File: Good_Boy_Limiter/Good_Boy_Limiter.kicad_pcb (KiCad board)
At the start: 2 copper layers, 7 parts, among them Q2 AO3422, U1 ESP32-S3-WROOM-1, U2 TC4427EOA_C636891, U3 XL7015E1

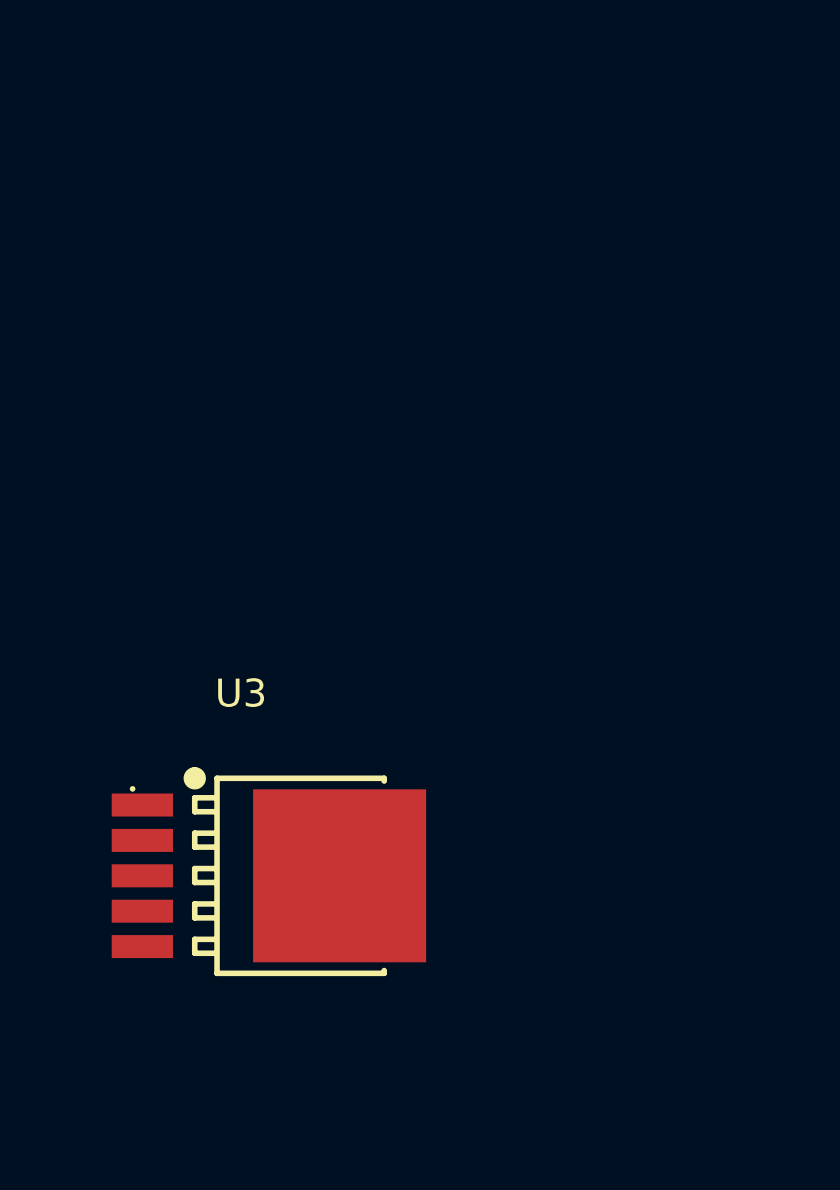
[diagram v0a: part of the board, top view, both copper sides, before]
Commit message: Added schottky and Inductor for DC-DC converter
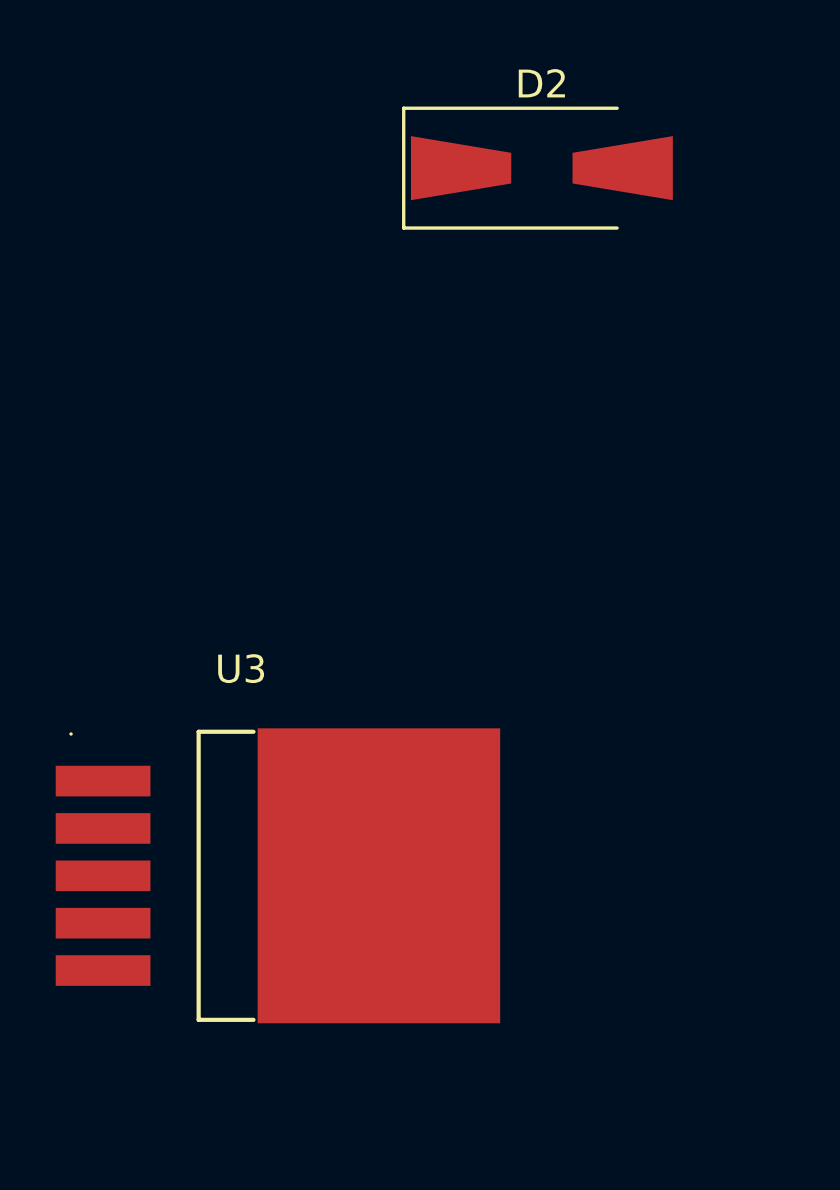
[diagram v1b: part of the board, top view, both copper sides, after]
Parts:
- added D2: SS36, Diode_SMD:D_SMA-SMB_Universal_Handsoldering, F.Cu at (47.9, 30.5)
- U3: value XL7015E1 -> LM2576HVR-12; footprint easyeda2kicad:TO-252-5_L6.6-W5.8-P1.27-TL -> easyeda2kicad:TO-263-5_L10.2-W8.6-P1.70-LS14.4-TL
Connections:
- C1 pad 1: unconnected-(C1-Pad1) -> /GPIO1
- C1 pad 2: unconnected-(C1-Pad2) -> GND
- Q2 pad 1: unconnected-(Q2-G-Pad1) -> Net-(Q2-G)
- Q2 pad 2: unconnected-(Q2-S-Pad2) -> +48VOUT
- Q2 pad 3: unconnected-(Q2-D-Pad3) -> Net-(Q2-D)
- R1 pad 1: unconnected-(R1-Pad1) -> GND
- R1 pad 2: unconnected-(R1-Pad2) -> /GPIO1
- R2 pad 2: unconnected-(R2-Pad2) -> /GPIO1
- U1 pad 1: Net-(U1-GND-Pad1) -> GND
- U1 pad 38: unconnected-(U1-IO2-Pad38) -> /GPIO2
- U1 pad 39: unconnected-(U1-IO1-Pad39) -> /GPIO1
- U1 pad 40: Net-(U1-GND-Pad1) -> GND
- U1 pad 41: Net-(U1-GND-Pad1) -> GND
- U2 pad 2: unconnected-(U2-INA-Pad2) -> /GPIO2
- U2 pad 3: unconnected-(U2-GND-Pad3) -> GND
- U2 pad 6: unconnected-(U2-VDD-Pad6) -> /+12V
- U2 pad 7: unconnected-(U2-OUTA-Pad7) -> Net-(U2-OUTA)
- U3 pad 1: unconnected-(U3-VIN-Pad1) -> +48VIN
- U3 pad 2: unconnected-(U3-SW-Pad2) -> Net-(D2-K)
- U3 pad 3: unconnected-(U3-GND-Pad3) -> GND
- U3 pad 4: unconnected-(U3-FB-Pad4) -> /+12V
- U3 pad 5: unconnected-(U3-EN-Pad5) -> GND
- U3 pad 6: unconnected-(U3-GND-Pad6) -> GND

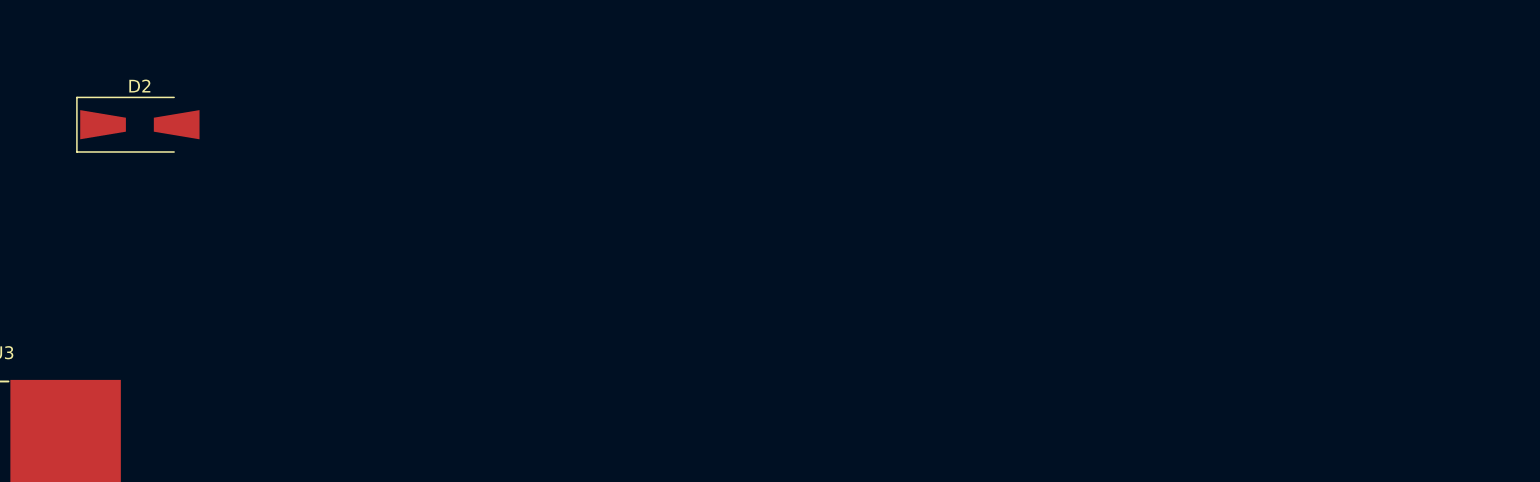
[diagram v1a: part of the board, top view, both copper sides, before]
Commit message: FIX: Added capacitors for Buck
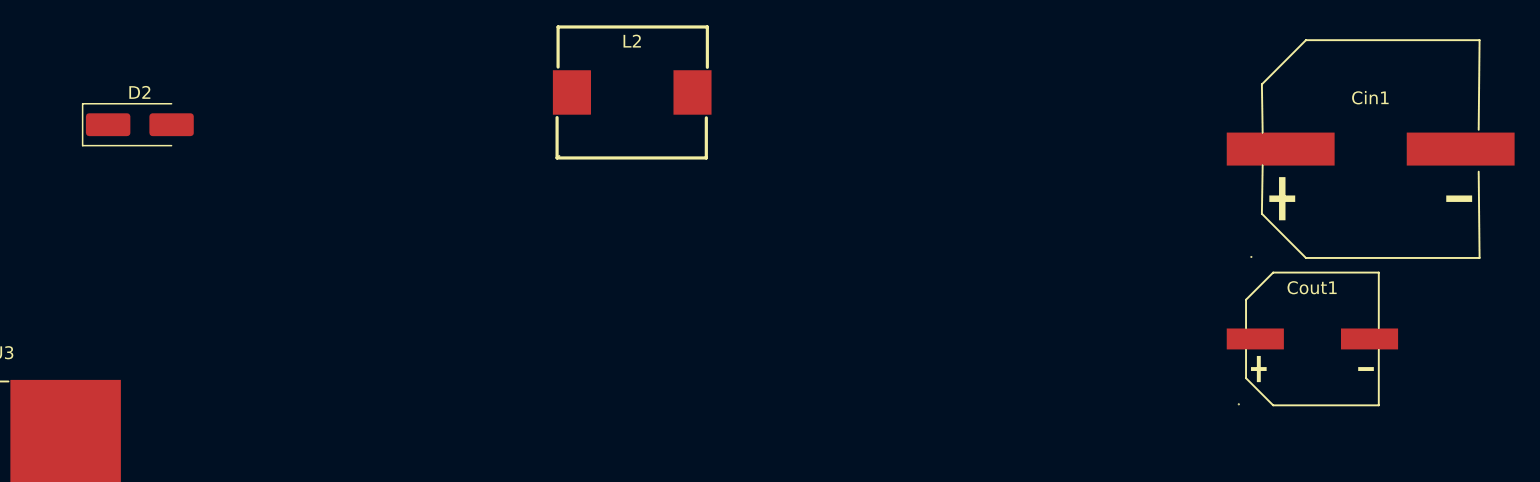
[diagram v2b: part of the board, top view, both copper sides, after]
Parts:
- added Cin1: 100uF, easyeda2kicad:CAP-SMD_BD16.0-L17.0-W17.0-FD, F.Cu at (144.9, 32.4)
- added Cout1: 1000uF, easyeda2kicad:CAP-SMD_BD10.0-L10.3-W10.3-FD, F.Cu at (140.3, 47.4)
- added L2: SL1050-101M, easyeda2kicad:IND-SMD_L11.5-W10.5, F.Cu at (86.7, 27.9)
- D2: footprint Diode_SMD:D_SMA-SMB_Universal_Handsoldering -> Diode_SMD:D_SMA_Handsoldering

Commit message: Added a lot of stuff, sowwy
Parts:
- added Cin2: 100uF, easyeda2kicad:CAP-SMD_BD16.0-L17.0-W17.0-FD, F.Cu at (57.0, 122.2)
- added Cout2: 1000uF, easyeda2kicad:CAP-SMD_BD10.0-L10.3-W10.3-FD, F.Cu at (69.2, 137.2)
- added D3: SS36, Diode_SMD:D_SMA_Handsoldering, F.Cu at (73.9, 126.9)
- added D4: 1N4148W, Diode_SMD:D_SOD-123, F.Cu at (133.5, 87.1)
- added D7: LED, LED_SMD:LED_0805_2012Metric_Pad1.15x1.40mm_HandSolder, F.Cu at (129.4, 97.3)
- added D8: LED, LED_SMD:LED_0805_2012Metric_Pad1.15x1.40mm_HandSolder, F.Cu at (129.4, 100.3)
- added L3: SL1050-101M, easyeda2kicad:IND-SMD_L11.5-W10.5, F.Cu at (75.6, 118.8)
- added U4: LM2576SX-3.3/NOPB, easyeda2kicad:TO-263-5_L10.2-W8.9-P1.70-TL, F.Cu at (52.3, 137.4)
- added U5: MAX40200AUK+T, easyeda2kicad:TSOT-23-5_L2.9-W1.6-P0.95-LS2.8-BL, F.Cu at (133.0, 90.9)
- added U6: AMS1117-3.3, Package_TO_SOT_SMD:SOT-223-3_TabPin2, F.Cu at (125.6, 89.6)
- added U7: MAX40200AUK+T, easyeda2kicad:TSOT-23-5_L2.9-W1.6-P0.95-LS2.8-BL, F.Cu at (136.2, 97.9)
- added U9: LM393DR2G, easyeda2kicad:SOIC-8_L5.0-W4.0-P1.27-LS6.0-BL, F.Cu at (123.8, 99.9)
- added USB1: USB-TYPE-C-018, easyeda2kicad:USB-C_SMD-TYPE-C-31-M-12, F.Cu at (126.1, 79.7)
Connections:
- U1 pad 13: unconnected-(U1-USB_D--Pad13) -> /D-
- U1 pad 14: unconnected-(U1-USB_D+-Pad14) -> /D+
- U1 pad 2: unconnected-(U1-3V3-Pad2) -> /3V3
- U1 pad 27: unconnected-(U1-IO0-Pad27) -> /GPIO0
- U1 pad 3: unconnected-(U1-EN-Pad3) -> Net-(U1-EN)

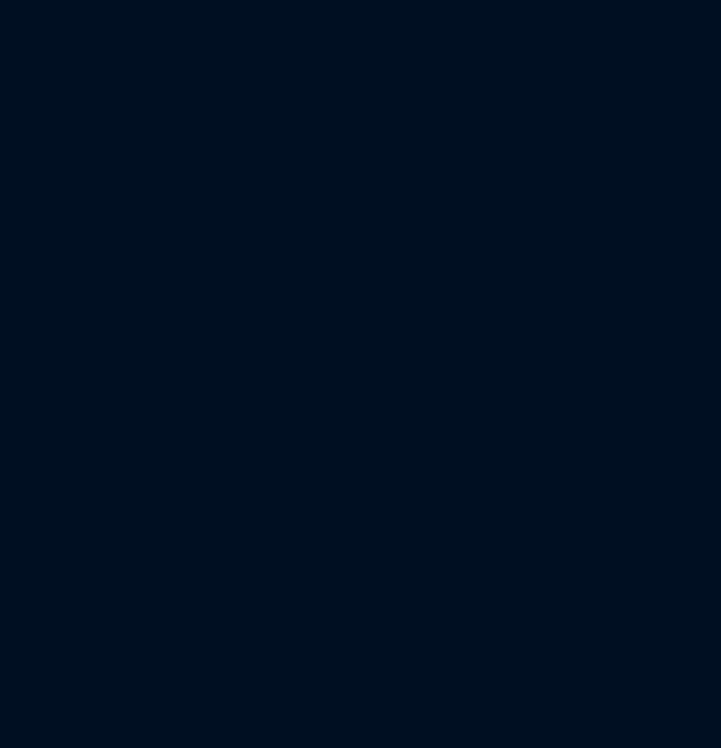
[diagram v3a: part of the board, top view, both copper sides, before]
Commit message: Added some footprints
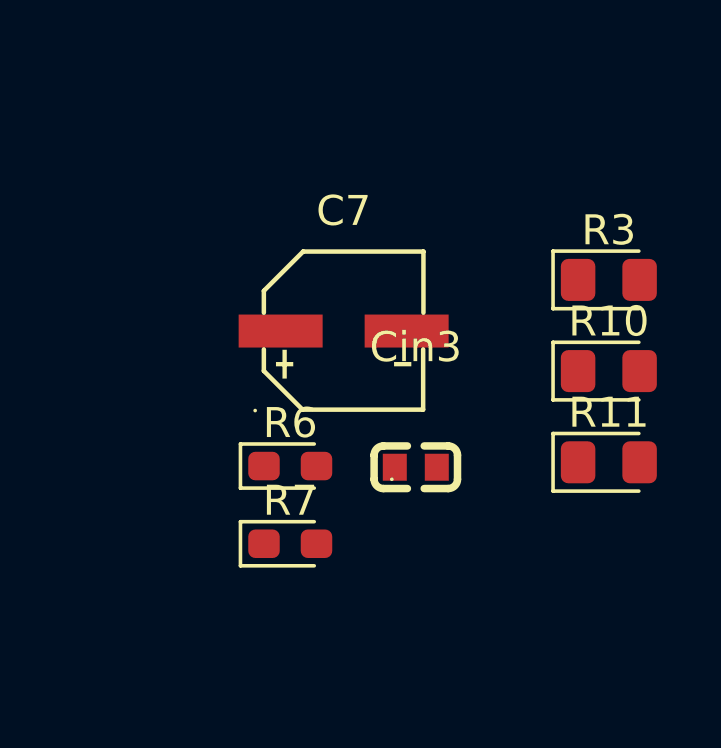
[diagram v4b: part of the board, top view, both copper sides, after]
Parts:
- added C7: 22uF, easyeda2kicad:CAP-SMD_BD5.0-L5.3-W5.3-FD, F.Cu at (165.4, 64.2)
- added Cin3: 10uF, easyeda2kicad:C0603, F.Cu at (167.8, 68.7)
- added R10: 330, LED_SMD:LED_0805_2012Metric_Pad1.15x1.40mm_HandSolder, F.Cu at (174.2, 65.5)
- added R11: 330, LED_SMD:LED_0805_2012Metric_Pad1.15x1.40mm_HandSolder, F.Cu at (174.2, 68.6)
- added R3: 10, LED_SMD:LED_0805_2012Metric_Pad1.15x1.40mm_HandSolder, F.Cu at (174.2, 62.5)
- added R6: 5.1K, LED_SMD:LED_0603_1608Metric_Pad1.05x0.95mm_HandSolder, F.Cu at (163.6, 68.7)
- added R7: 5.1K, LED_SMD:LED_0603_1608Metric_Pad1.05x0.95mm_HandSolder, F.Cu at (163.6, 71.3)

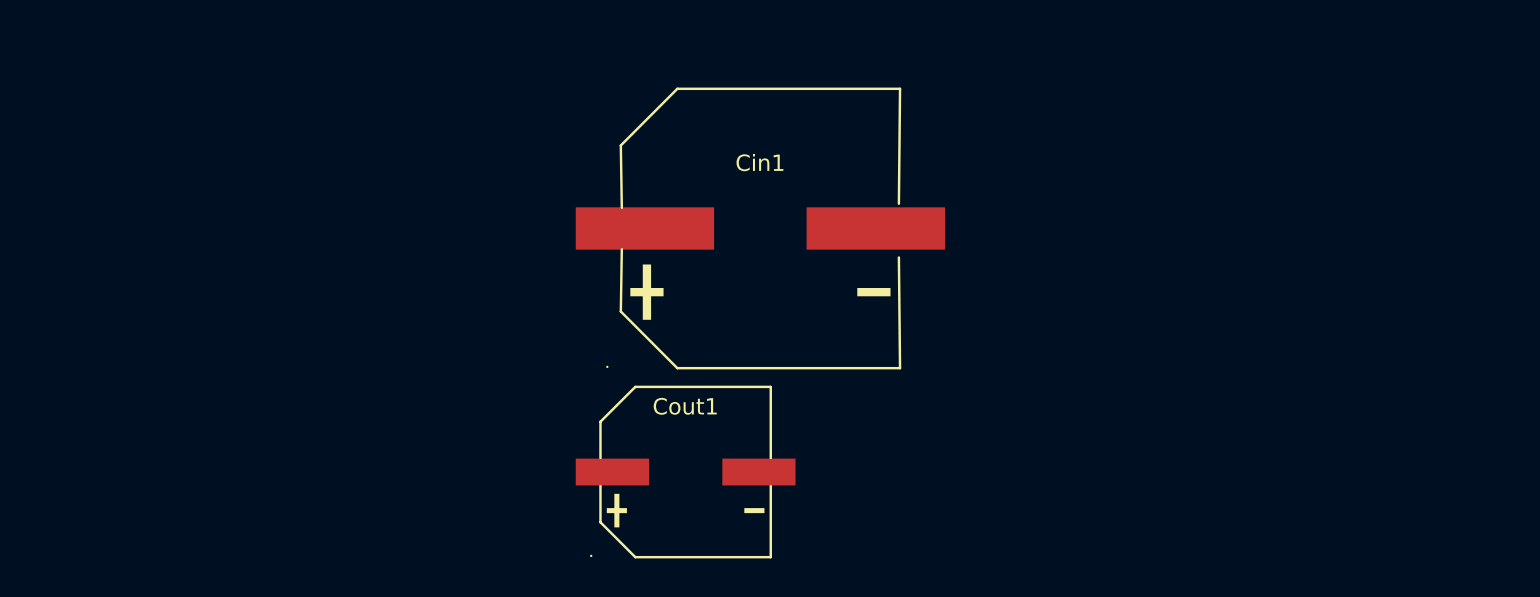
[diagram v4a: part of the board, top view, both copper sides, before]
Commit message: Added more footprints
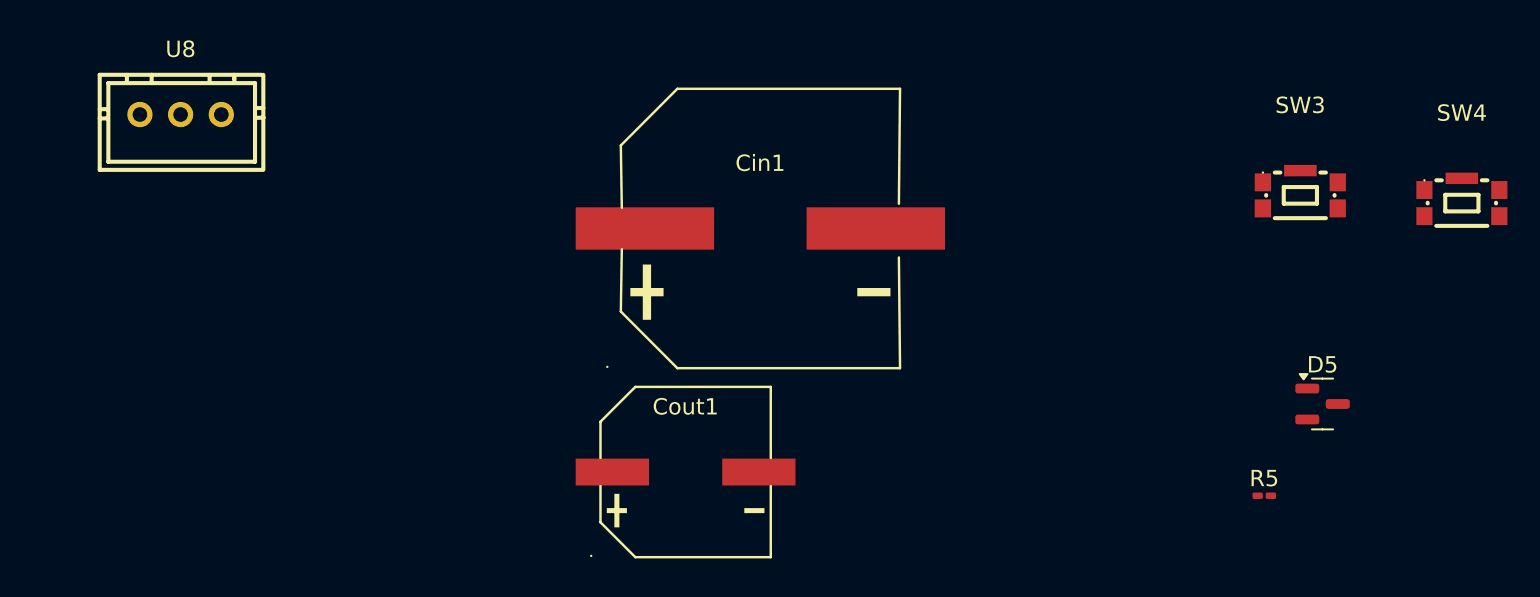
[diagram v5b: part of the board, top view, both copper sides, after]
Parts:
- added D5: 3V3, Package_TO_SOT_SMD:SOT-23, F.Cu at (179.4, 43.2)
- added R5: 10k, Resistor_SMD:R_0201_0603Metric_Pad0.64x0.40mm_HandSolder, F.Cu at (175.8, 48.8)
- added SW3: RESET1, easyeda2kicad:KEY-SMD_KMR2XXGXXX, F.Cu at (178.0, 30.0)
- added SW4: BOOT1, easyeda2kicad:KEY-SMD_KMR2XXGXXX, F.Cu at (188.0, 30.5)
- added U8: B3B-XH-A, easyeda2kicad:CONN-TH_3P-P2.50_A2501WV2-3P, F.Cu at (109.3, 25.4)
- R1: value 47k -> 100k
- R2: value 2.2k -> 4.7k
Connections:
- R2 pad 1: unconnected-(R2-Pad1) -> /V_Sensing
